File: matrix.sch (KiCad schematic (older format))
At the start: 153 parts

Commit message: Remap project symbols
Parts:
- D01, D02, D03, D04, D05, D06, D07, D08, D09, D10, D11, D12, D13, D14, D15, D16, D17, D18, D19, D21, D22, D23, D24, D26, D27, D28, D29, D30, D31, D32, D33, D34, D36, D37, D38, D39, D41, D42, D43, D44, D46, D47, D48, D49, D50, D51, D52, D53, D54, D55, D56, D57, D58, D59, D60, D61, D62, D63, D64, D65, D66, D67, D68, D69, D70: symbol DIODE -> device:DIODE
- DC1, DC2, DC3: symbol LED -> device:LED
- R4: symbol R -> device:R
- S01, S02, S03, S031, S04, S041, S05, S0512, S06, S07, S08, S09, S10, S101, S102, S11, S12, S13, S14, S15, S151, S16, S17, S18, S19, S21, S22, S23, S24, S26, S27, S28, S29, S30, S301, S302, S31, S32, S33, S34, S36, S37, S38, S39, S41, S42, S43, S44, S46, S47, S48, S49, S50, S51, S52, S53, S54, S55, S552, S56, S57, S58, S59, S60, S601, S602, S61, S62, S63, S64, S641, S65, S6512, S66, S661, S67, S68, S681, S682, S69, S691, S692, S70, S7012: symbol MX1A -> mx1a-simple:MX1A

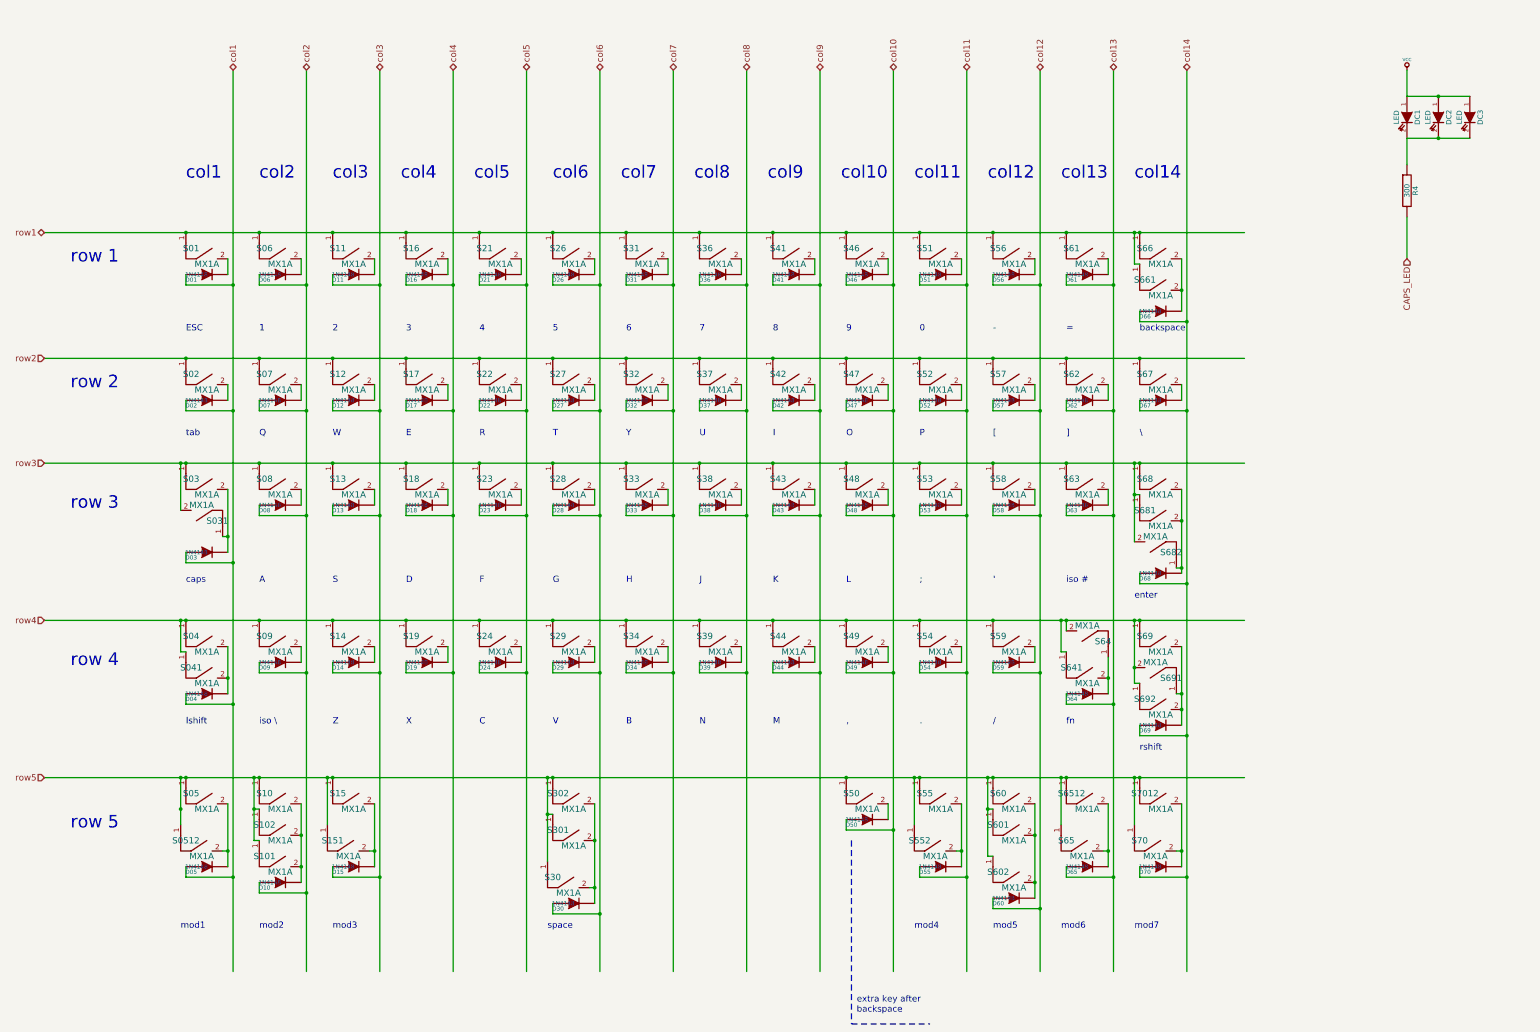
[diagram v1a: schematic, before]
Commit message: Remove SW50 from matrix and leds
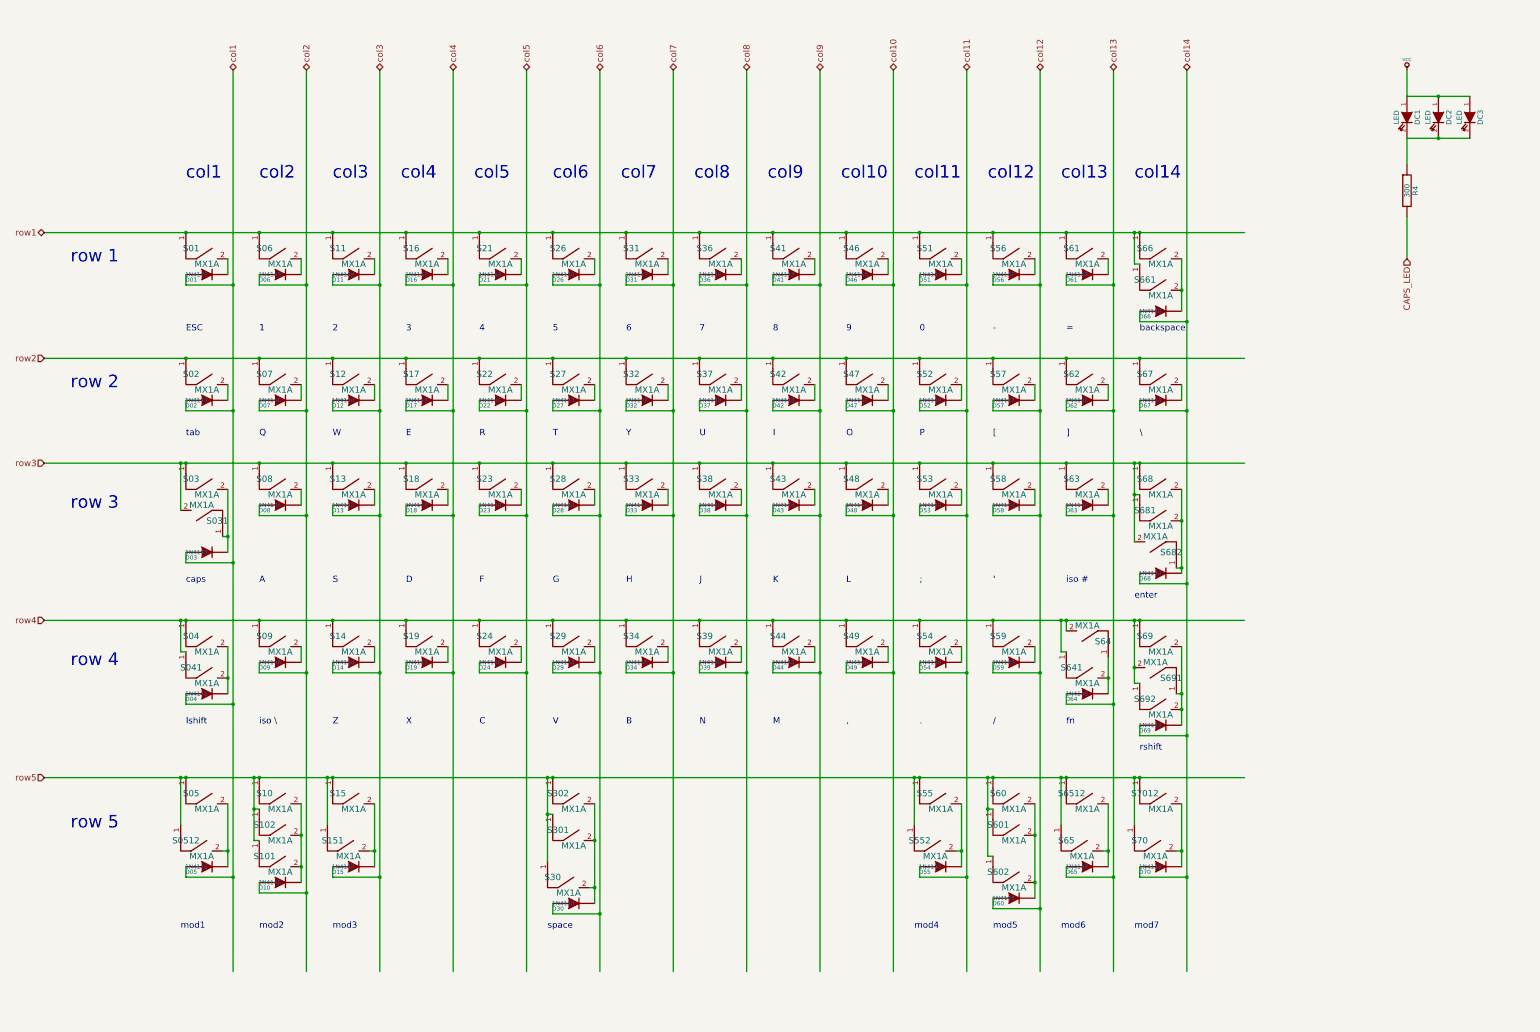
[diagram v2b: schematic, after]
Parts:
- removed D50: 1N4148, 0805:0805D, symbol device:DIODE
- removed S50: MX1A, mx1a:MX1A_no3d, symbol mx1a-simple:MX1A
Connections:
- wire segments 254 -> 418
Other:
- note removed: "extra key after\nbackspace"

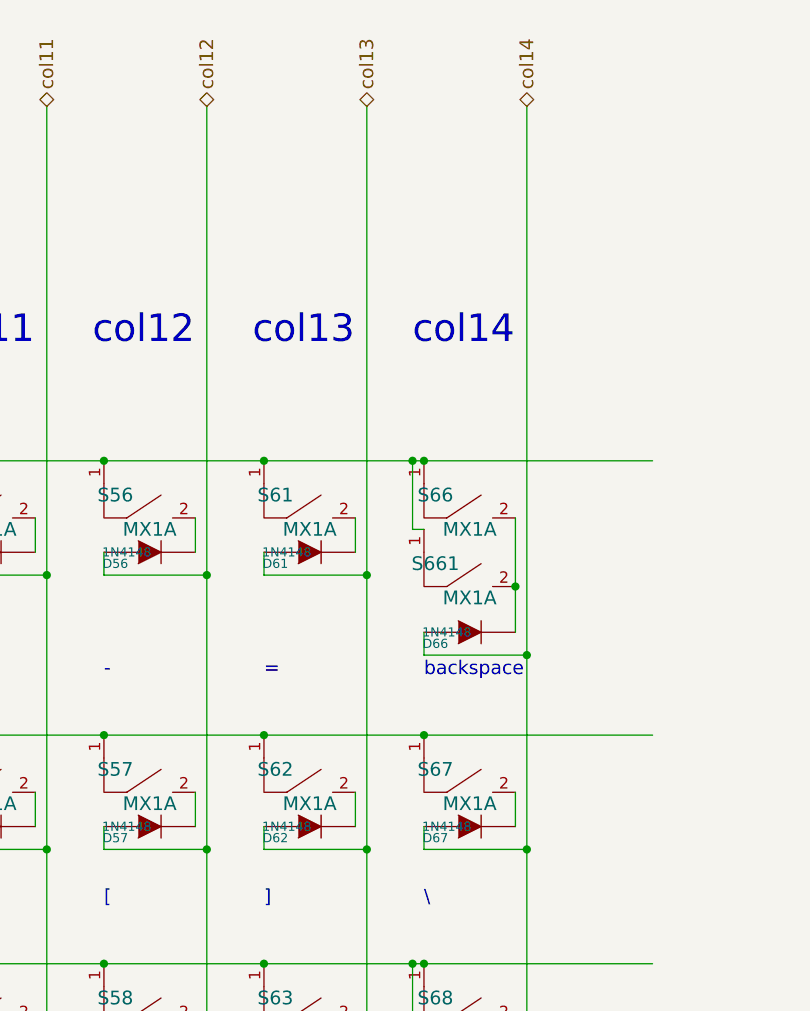
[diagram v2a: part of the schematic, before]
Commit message: Remove SW661
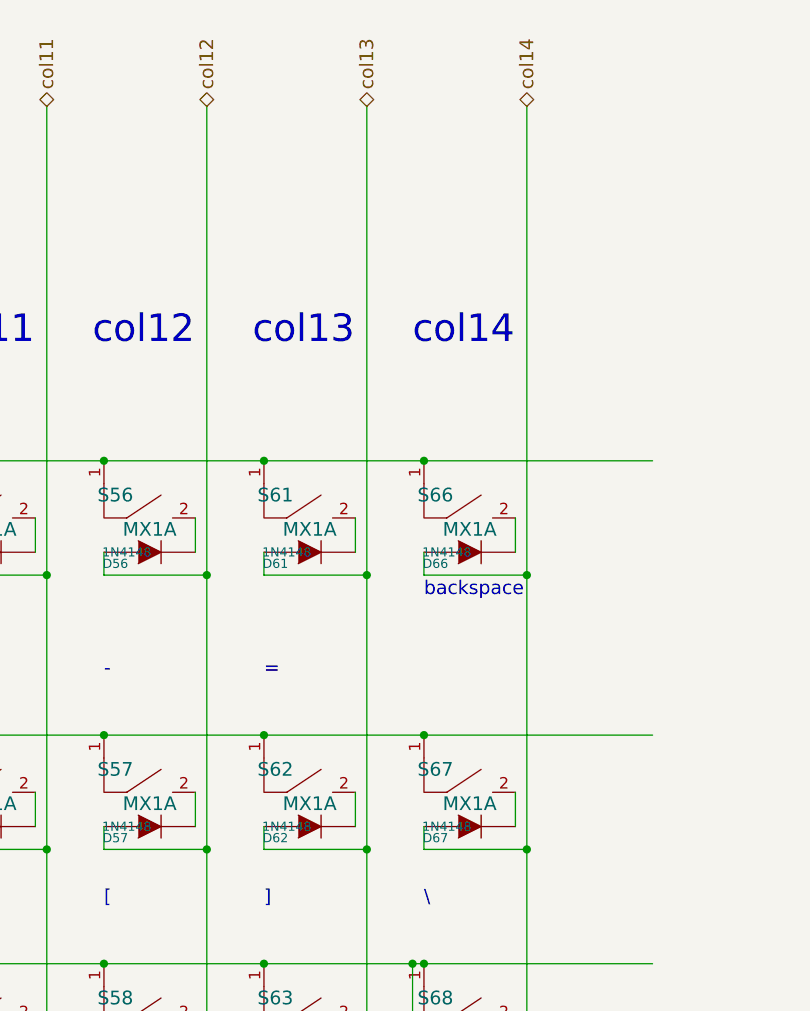
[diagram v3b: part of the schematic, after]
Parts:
- removed S661: MX1A, mx1a:MX1A_no3d, symbol mx1a-simple:MX1A
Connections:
- wire segments 418 -> 414
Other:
- moved on the sheet: D66
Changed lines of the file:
@@
 L device:DIODE D66
 U 1 1 506B5A55
-P 12450 3700
-F 0 "D66" H 12300 3650 40  0000 C CNN
-F 1 "1N4148" H 12350 3700 40  0000 C CNN
-F 2 "0805:0805D" H 12450 3700 60  0001 C CNN
-F 3 "" H 12450 3700 60  0001 C CNN
-F 4 "DC Components" H 5300 3700 60  0001 C CNN "Vendor"
-F 5 "CD4148WS(0805C)" H 5300 3700 60  0001 C CNN "Product"
-F 6 "TME" H 5300 3700 60  0001 C CNN "Supplier"
-F 7 "1N4148-0805" H 5300 3700 60  0001 C CNN "Supplier Symbol"
-	1    12450 3700
+P 12450 3350
+F 0 "D66" H 12300 3300 40  0000 C CNN
+F 1 "1N4148" H 12350 3350 40  0000 C CNN
+F 2 "0805:0805D" H 12450 3350 60  0001 C CNN
+F 3 "" H 12450 3350 60  0001 C CNN
+F 4 "DC Components" H 5300 3350 60  0001 C CNN "Vendor"
+F 5 "CD4148WS(0805C)" H 5300 3350 60  0001 C CNN "Product"
+F 6 "TME" H 5300 3350 60  0001 C CNN "Supplier"
+F 7 "1N4148-0805" H 5300 3350 60  0001 C CNN "Supplier Symbol"
+	1    12450 3350
 	1    0    0    -1
 $EndComp
@@
 Text Notes 11550 3900 0    60   ~ 0
 =
-Text Notes 12250 3900 0    60   ~ 0
+Text Notes 12250 3550 0    60   ~ 0
 backspace
 Text Notes 3150 4900 0    60   ~ 0
@@
 Text Notes 12200 9600 0    60   ~ 0
 mod7
-$Comp
-L mx1a-simple:MX1A S661
-U 1 1 51374D98
-P 12450 3650
-F 0 "S661" H 12300 3900 60  0000 C CNN
-F 1 "MX1A" H 12450 3750 60  0000 C CNN
-F 2 "mx1a:MX1A_no3d" H 12450 3650 60  0001 C CNN
-F 3 "" H 12450 3650 60  0001 C CNN
-	1    12450 3650
-	1    0    0    -1
-$EndComp
 Wire Wire Line
 	4300 1400 4300 3450
@@
 	7800 1400 7800 3450
 Wire Wire Line
-	12700 1400 12700 3800
+	12700 1400 12700 3450
 Wire Wire Line
 	5950 3350 5950 3450
@@
 	11250 4550 11250 4400
 Wire Wire Line
-	12250 3800 12700 3800
-Wire Wire Line
-	12650 3200 12650 3500
+	12250 3450 12700 3450
 Wire Wire Line
 	11550 3350 11550 3450
@@
 Connection ~ 11300 3450
 Connection ~ 12000 3450
-Connection ~ 12700 3800
 Connection ~ 12700 4650
 Connection ~ 12000 4650
@@
 	10800 8900 10850 8900
 Wire Wire Line
-	12250 3800 12250 3700
-Wire Wire Line
-	12250 3250 12200 3250
-Wire Wire Line
-	12200 3250 12200 2950
-Connection ~ 12200 2950
-Connection ~ 12650 3500
+	12250 3450 12250 3350
 Wire Wire Line
 	3850 8450 3800 8450
@@
 	12250 2950 13250 2950
 Wire Wire Line
-	11550 2950 12200 2950
-Wire Wire Line
 	10850 2950 11550 2950
 Wire Wire Line
@@
 	12000 3450 12000 4650
 Wire Wire Line
-	12700 3800 12700 4650
-Wire Wire Line
 	12700 4650 12700 6300
 Wire Wire Line
@@
 	12650 7500 12650 7650
 Wire Wire Line
-	12200 2950 12250 2950
-Wire Wire Line
-	12650 3500 12650 3700
-Wire Wire Line
 	3800 8450 3800 8750
 Wire Wire Line
@@
 Wire Wire Line
 	9900 7150 9900 10000
+Wire Wire Line
+	12650 3200 12650 3350
+Wire Wire Line
+	11550 2950 12250 2950
+Connection ~ 12700 3450
+Wire Wire Line
+	12700 3450 12700 4650
 $EndSCHEMATC

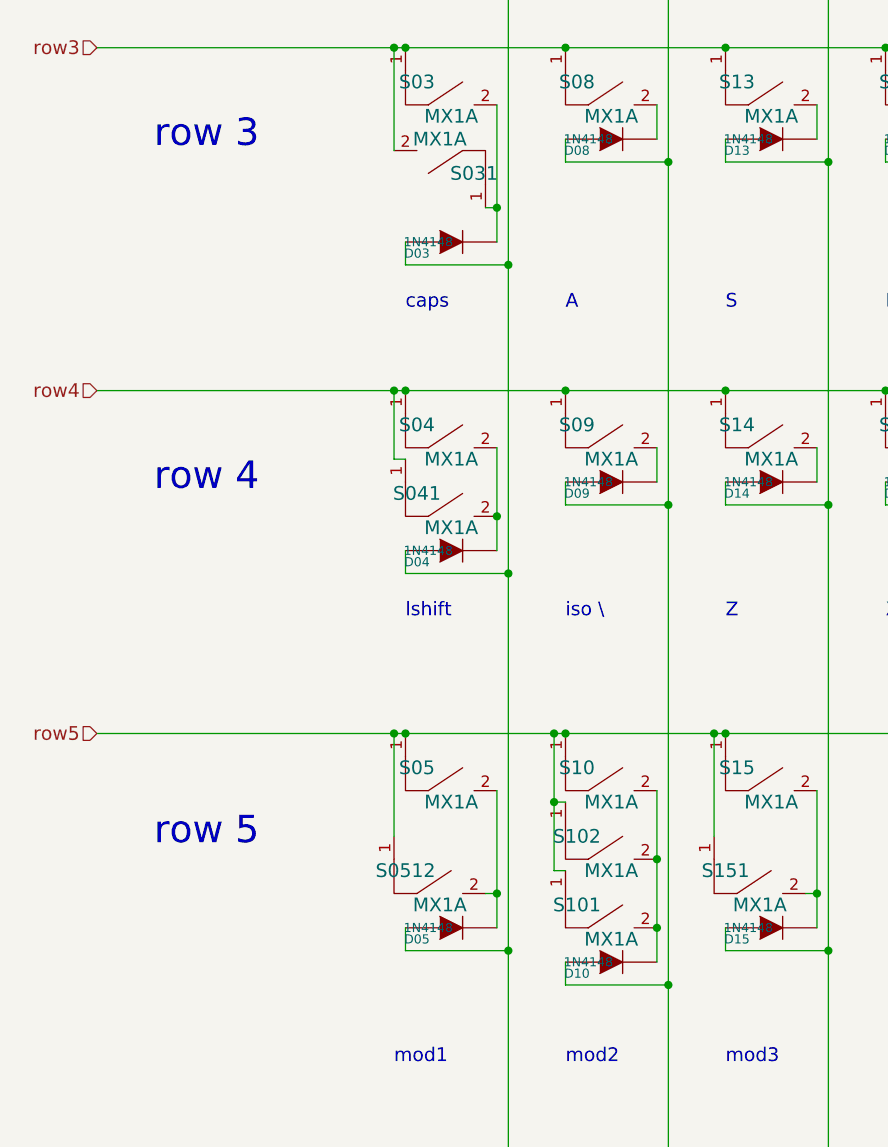
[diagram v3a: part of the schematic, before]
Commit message: Remove SW09 and SW041
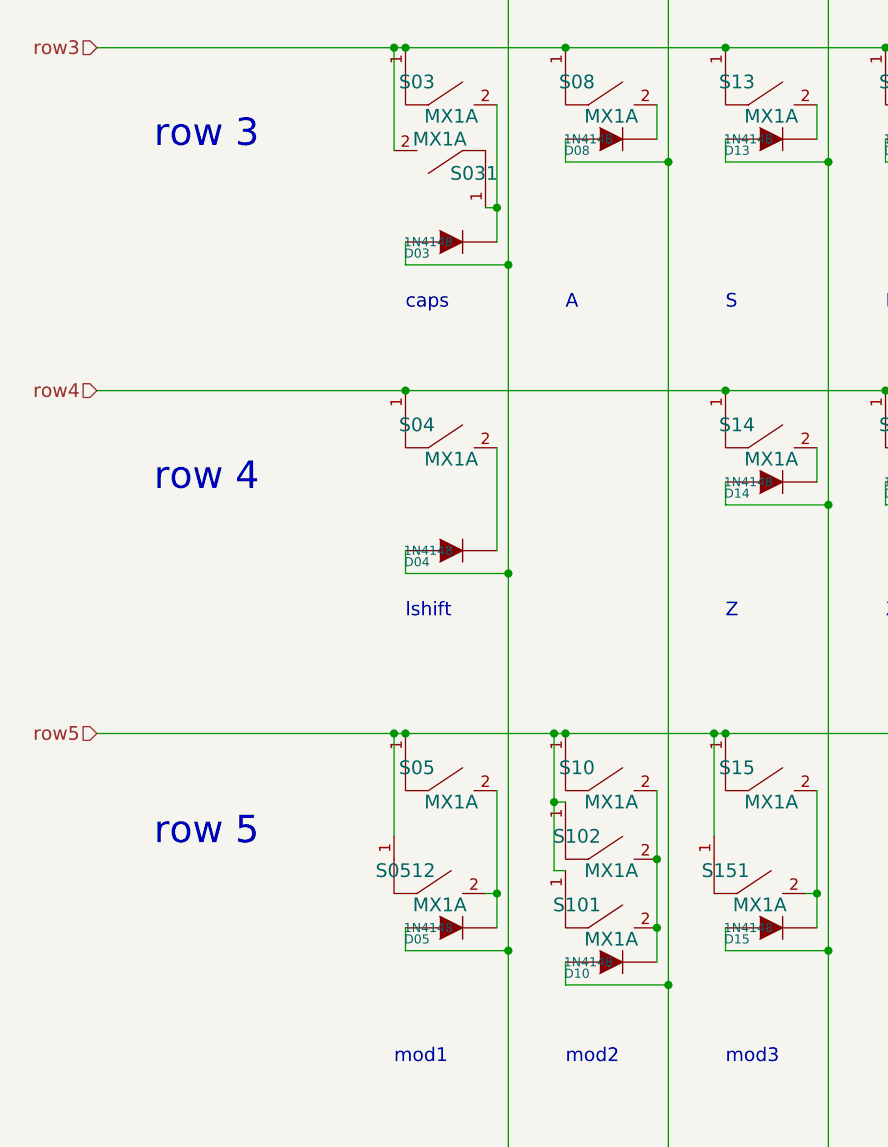
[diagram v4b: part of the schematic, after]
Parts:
- removed D09: 1N4148, 0805:0805D, symbol device:DIODE
- removed S041, S09: MX1A, mx1a:MX1A_no3d, symbol mx1a-simple:MX1A
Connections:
- wire segments 414 -> 405
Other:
- note removed: "iso \"
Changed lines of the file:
@@
-$EndComp
-$Comp
-L mx1a-simple:MX1A S09
-U 1 1 5040DEBD
-P 4050 7050
-F 0 "S09" H 3900 7300 60  0000 C CNN
-F 1 "MX1A" H 4050 7150 60  0000 C CNN
-F 2 "mx1a:MX1A_no3d" H 4050 7050 60  0001 C CNN
-F 3 "" H 4050 7050 60  0001 C CNN
-	1    4050 7050
-	1    0    0    -1
 $EndComp
 $Comp
@@
 F 3 "" H 6850 8550 60  0001 C CNN
 	1    6850 8550
-	1    0    0    -1
-$EndComp
-$Comp
-L mx1a-simple:MX1A S041
-U 1 1 50410564
-P 3350 7350
-F 0 "S041" H 3200 7600 60  0000 C CNN
-F 1 "MX1A" H 3350 7450 60  0000 C CNN
-F 2 "mx1a:MX1A_no3d" H 3350 7350 60  0001 C CNN
-F 3 "" H 3350 7350 60  0001 C CNN
-	1    3350 7350
 	1    0    0    -1
 $EndComp
@@
 $EndComp
 $Comp
-L device:DIODE D04
-U 1 1 506B1C3D
-P 3350 7350
-F 0 "D04" H 3200 7300 40  0000 C CNN
-F 1 "1N4148" H 3250 7350 40  0000 C CNN
-F 2 "0805:0805D" H 3350 7350 60  0001 C CNN
-F 3 "" H 3350 7350 60  0001 C CNN
-F 4 "DC Components" H 3350 4750 60  0001 C CNN "Vendor"
-F 5 "CD4148WS(0805C)" H 3350 4750 60  0001 C CNN "Product"
-F 6 "TME" H 3350 4750 60  0001 C CNN "Supplier"
-F 7 "1N4148-0805" H 3350 4750 60  0001 C CNN "Supplier Symbol"
-	1    3350 7350
-	1    0    0    -1
-$EndComp
-$Comp
 L device:DIODE D07
 U 1 1 506B1C46
@@
 F 7 "1N4148-0805" H 3650 4350 60  0001 C CNN "Supplier Symbol"
 	1    4750 5550
-	1    0    0    -1
-$EndComp
-$Comp
-L device:DIODE D09
-U 1 1 506B428A
-P 4050 7050
-F 0 "D09" H 3900 7000 40  0000 C CNN
-F 1 "1N4148" H 3950 7050 40  0000 C CNN
-F 2 "0805:0805D" H 4050 7050 60  0001 C CNN
-F 3 "" H 4050 7050 60  0001 C CNN
-F 4 "DC Components" H 3500 4750 60  0001 C CNN "Vendor"
-F 5 "CD4148WS(0805C)" H 3500 4750 60  0001 C CNN "Product"
-F 6 "TME" H 3500 4750 60  0001 C CNN "Supplier"
-F 7 "1N4148-0805" H 3500 4750 60  0001 C CNN "Supplier Symbol"
-	1    4050 7050
 	1    0    0    -1
 $EndComp
@@
 Text Notes 12200 6450 0    60   ~ 0
 enter
-Text Notes 3150 7650 0    60   ~ 0
-lshift
-Text Notes 3850 7650 0    60   ~ 0
-iso \
 Text Notes 4550 7650 0    60   ~ 0
 Z
@@
 Connection ~ 6650 6650
 Connection ~ 4550 6650
-Connection ~ 3850 6650
 Connection ~ 3150 6650
-Wire Wire Line
-	1800 6650 3100 6650
 Connection ~ 3150 5150
 Connection ~ 3850 5150
@@
 Wire Wire Line
 	12000 1400 12000 3450
-Connection ~ 3100 6650
 Wire Wire Line
 	11500 6650 11500 6950
@@
 	3550 4400 3550 4550
 Wire Wire Line
-	3150 7350 3150 7450
-Wire Wire Line
-	3150 7450 3600 7450
-Wire Wire Line
 	3850 4550 3850 4650
 Wire Wire Line
@@
 Wire Wire Line
 	4950 5550 4950 5400
-Wire Wire Line
-	3850 7050 3850 7150
-Wire Wire Line
-	3850 7150 4300 7150
-Wire Wire Line
-	4250 7050 4250 6900
 Wire Wire Line
 	4550 7050 4550 7150
@@
 Connection ~ 5000 5650
 Connection ~ 5000 7150
-Connection ~ 4300 7150
-Connection ~ 3600 7450
 Connection ~ 3600 9100
 Connection ~ 4300 9250
@@
 Connection ~ 9200 7150
 Wire Wire Line
-	3100 6650 3100 6950
-Wire Wire Line
-	3100 6950 3150 6950
-Wire Wire Line
-	3550 6900 3550 7200
-Connection ~ 3550 7200
-Wire Wire Line
 	12650 5400 12650 5700
 Connection ~ 12650 5700
@@
 	4550 6650 5250 6650
 Wire Wire Line
-	3850 6650 4550 6650
-Wire Wire Line
-	3150 6650 3850 6650
-Wire Wire Line
 	3150 5150 3850 5150
 Wire Wire Line
@@
 	11250 8700 11250 9150
 Wire Wire Line
-	3100 6650 3150 6650
-Wire Wire Line
 	11500 6650 11550 6650
 Wire Wire Line
@@
 	3600 4650 3600 6100
 Wire Wire Line
-	3600 6100 3600 7450
-Wire Wire Line
-	4300 5650 4300 7150
-Wire Wire Line
 	5000 5650 5000 7150
 Wire Wire Line
 	5000 7150 5000 9100
 Wire Wire Line
-	4300 7150 4300 9250
-Wire Wire Line
-	3600 7450 3600 9100
-Wire Wire Line
 	3600 9100 3600 10000
 Wire Wire Line
@@
 Wire Wire Line
 	9200 7150 9200 10000
-Wire Wire Line
-	3550 7200 3550 7350
 Wire Wire Line
 	12650 5700 12650 6150
@@
 Wire Wire Line
 	12700 3450 12700 4650
+Wire Wire Line
+	3150 6650 4550 6650
+Wire Wire Line
+	4300 5650 4300 9250
+Wire Wire Line
+	3600 7450 3600 9100
+Wire Wire Line
+	3600 6100 3600 7450
+Connection ~ 3600 7450
+Wire Wire Line
+	3150 7450 3600 7450
+Wire Wire Line
+	3150 7350 3150 7450
+Text Notes 3150 7650 0    60   ~ 0
+lshift
+$Comp
+L device:DIODE D04
+U 1 1 506B1C3D
+P 3350 7350
+F 0 "D04" H 3200 7300 40  0000 C CNN
+F 1 "1N4148" H 3250 7350 40  0000 C CNN
+F 2 "0805:0805D" H 3350 7350 60  0001 C CNN
+F 3 "" H 3350 7350 60  0001 C CNN
+F 4 "DC Components" H 3350 4750 60  0001 C CNN "Vendor"
+F 5 "CD4148WS(0805C)" H 3350 4750 60  0001 C CNN "Product"
+F 6 "TME" H 3350 4750 60  0001 C CNN "Supplier"
+F 7 "1N4148-0805" H 3350 4750 60  0001 C CNN "Supplier Symbol"
+	1    3350 7350
+	1    0    0    -1
+$EndComp
+Wire Wire Line
+	3550 6900 3550 7350
+Wire Wire Line
+	1800 6650 3150 6650
 $EndSCHEMATC
